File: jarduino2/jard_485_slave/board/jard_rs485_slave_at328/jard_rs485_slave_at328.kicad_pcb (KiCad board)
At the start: 2 copper layers, 80 x 30 mm, 66 parts, among them J1 BUS_IN, J2 BUS_OUT, J3 Débit, J4 Niveaux, J6 EV1, J7 ISCP, Q4 BPC_FMMT38C, Q6 P03P4L-04, U1 BPC_Alim5V, U2 MAX485E, U5 ATmega328P-A, U6 BPC_DHT22, Y1 Resonator

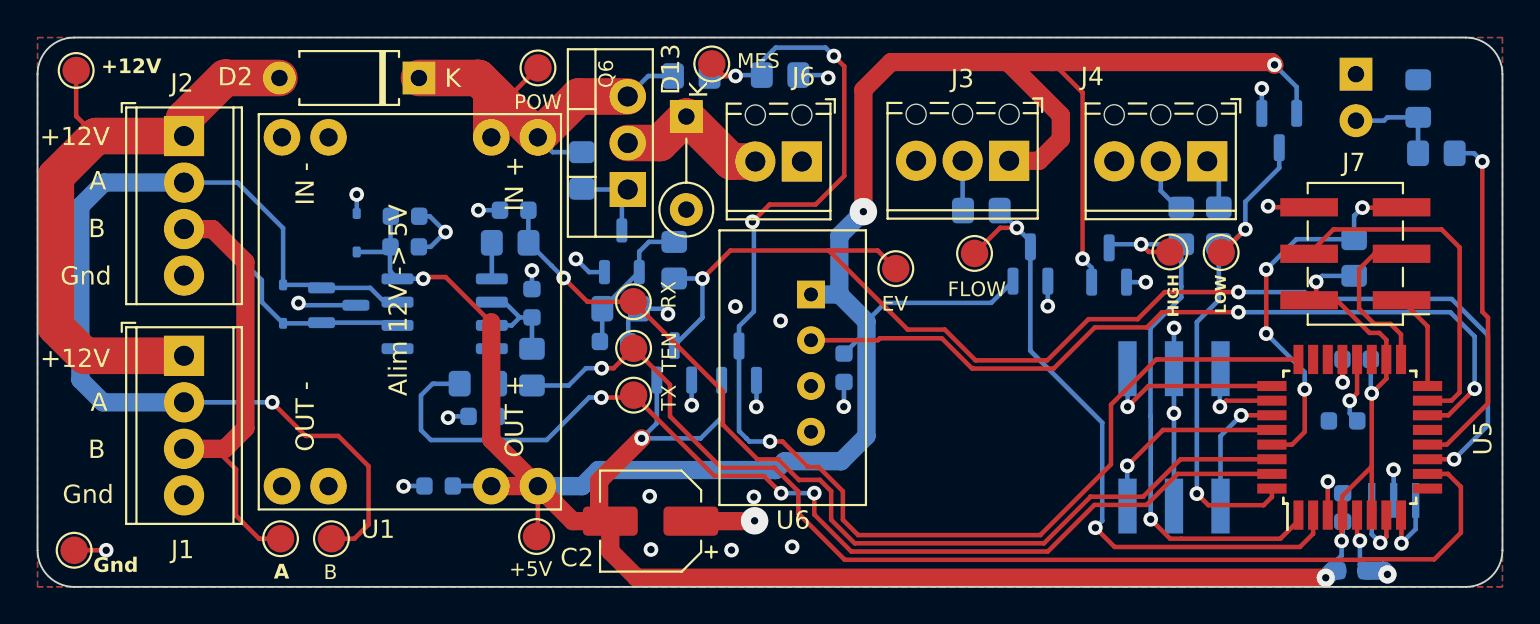
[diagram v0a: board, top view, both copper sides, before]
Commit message: Changement empreinte de D2 (trous + gros et 12mm long) Dessin sérigraphie J2 (sens de la sonde)
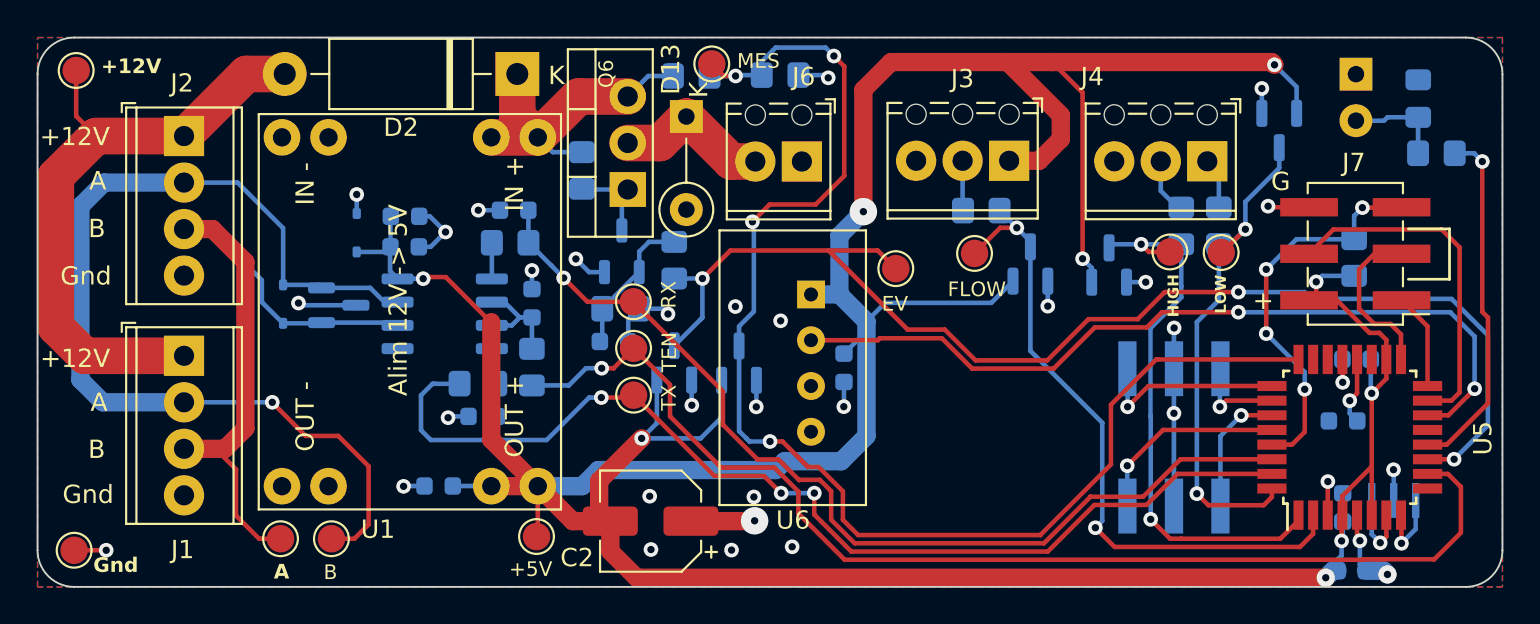
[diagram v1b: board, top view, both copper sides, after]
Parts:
- removed TP5: TestPoint, TestPoint:TestPoint_Pad_D1.5mm
- C8: value 1nF -> 100nF
- C9: value 100nF -> 1nF
- D13: value D -> 1N4007G
- D2: footprint Diode_THT:D_A-405_P7.62mm_Horizontal -> Diode_THT:D_DO-15_P12.70mm_Horizontal
- moved D2 5.37 mm to (139.6, 88.8)
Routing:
- net POWER_12V: track 26.4 -> 18.0 mm
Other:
- board text added: "+"
- board text added: "G"
- board text removed: "POW"
